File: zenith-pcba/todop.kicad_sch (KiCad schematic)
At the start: 1 part, among them U1 XC7A50T-CSG325

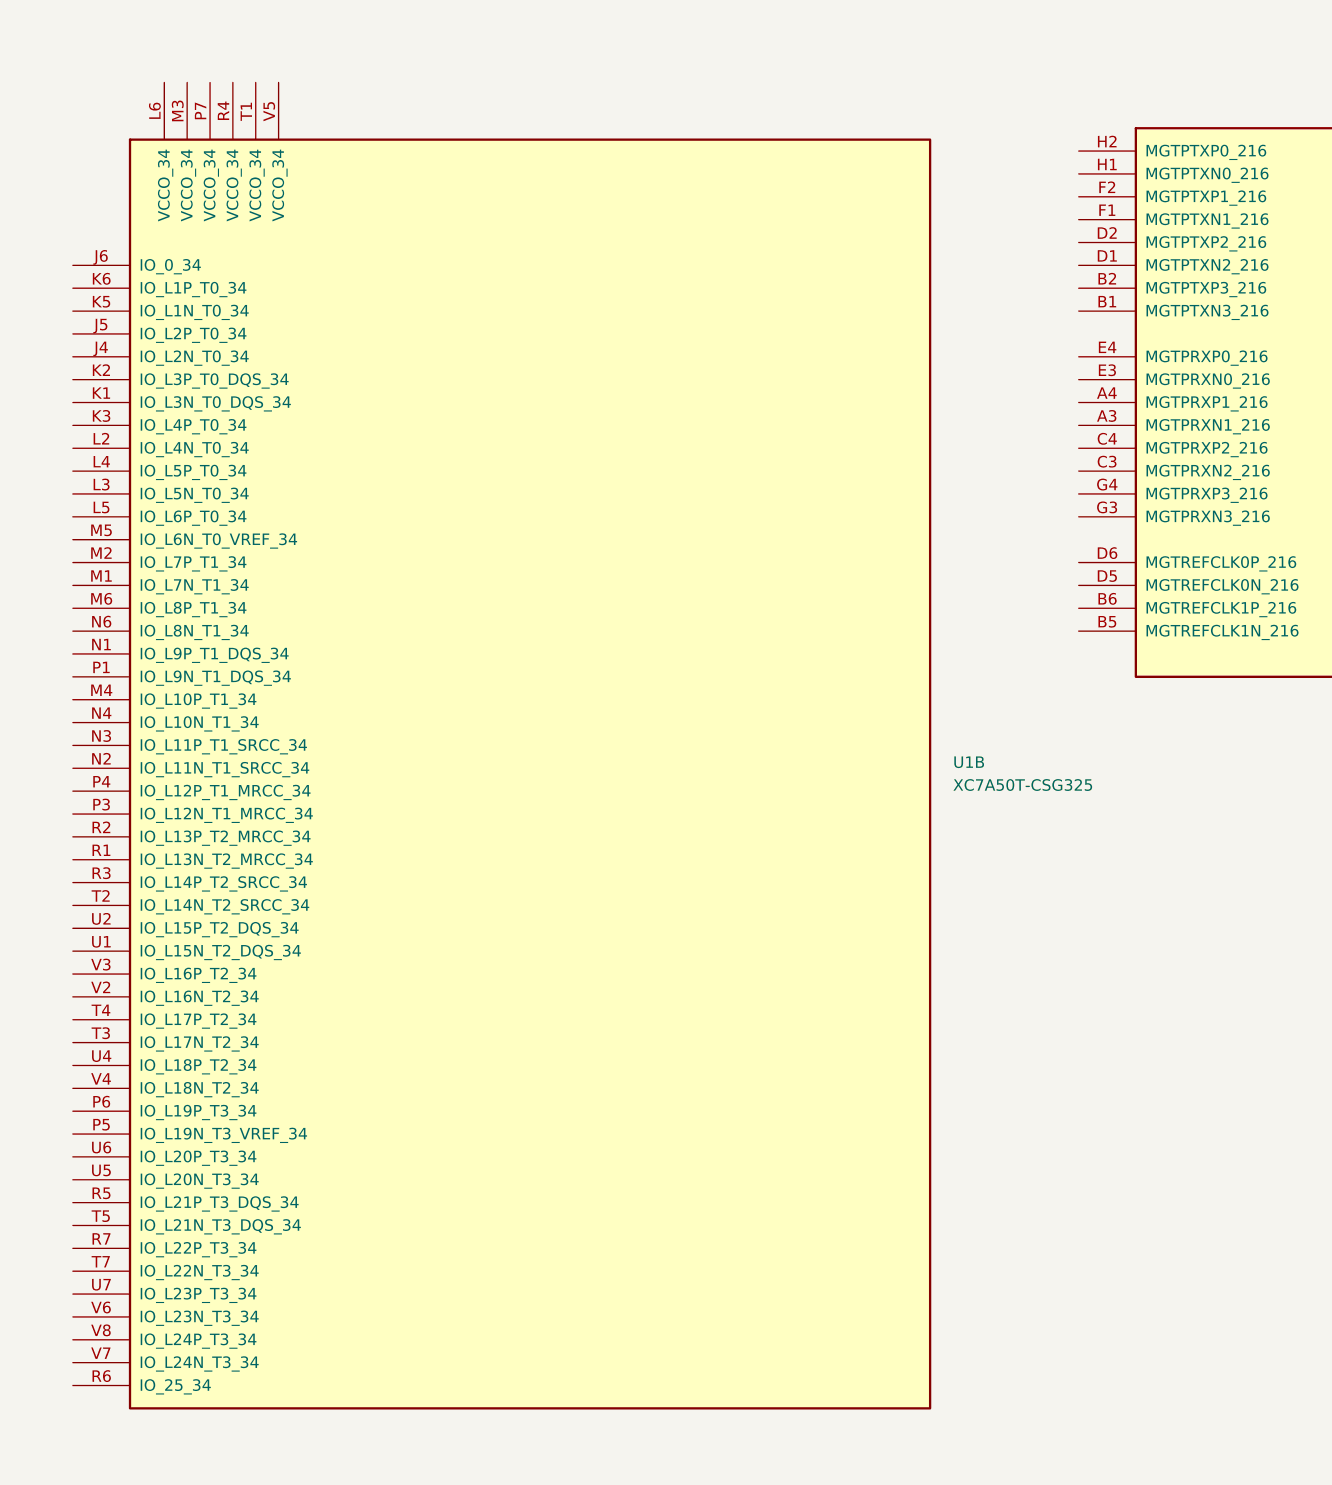
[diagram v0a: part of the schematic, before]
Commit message: feat(pcba): programmer connections and uart
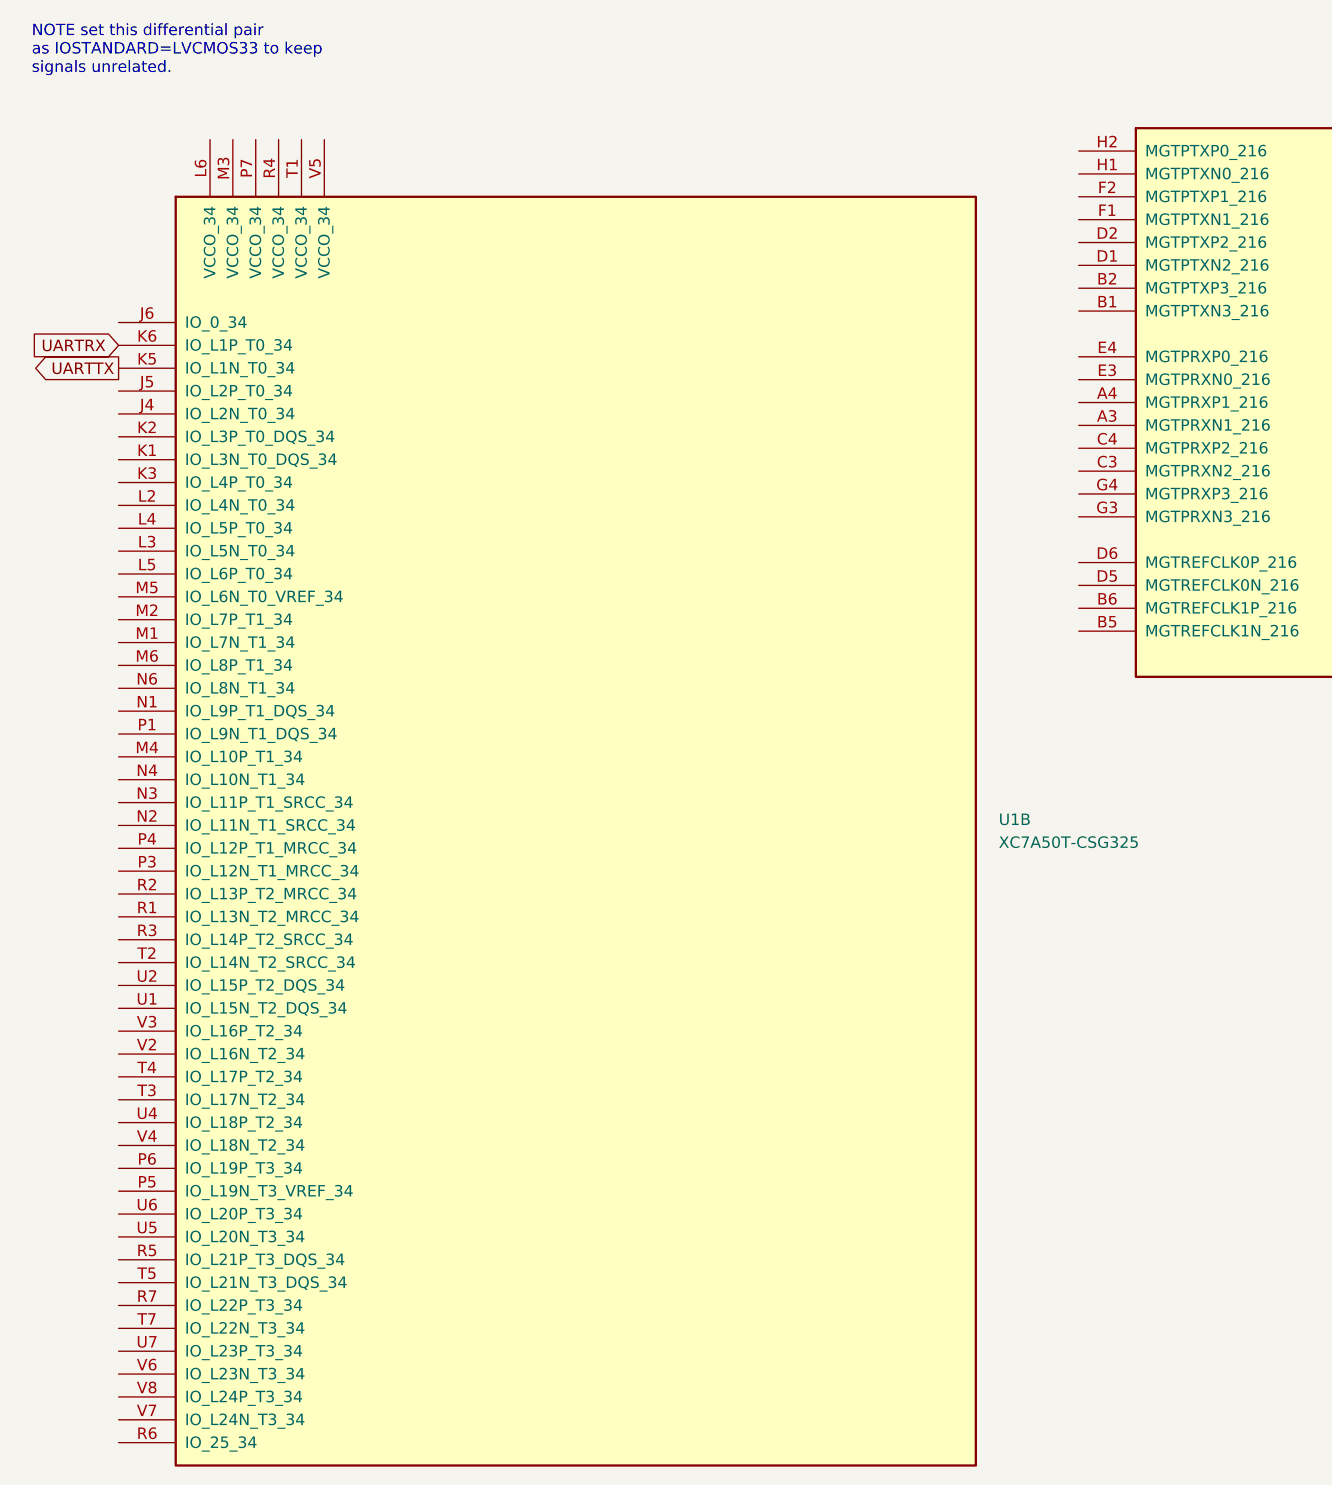
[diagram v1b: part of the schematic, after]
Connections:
- net UARTTX: now reaches U1.K5 (IO_L1N_T0_34)
- net UARTRX: now reaches U1.K6 (IO_L1P_T0_34)
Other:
- note added: "NOTE set this differential pair as IOSTANDARD=LVCMOS33 to keep signals unrelated."
- moved on the sheet: U1B
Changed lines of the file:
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@@
 	(generator_version "10.0")
 	(paper "A4")
+	(text "NOTE set this differential pair\nas IOSTANDARD=LVCMOS33 to keep\nsignals unrelated."
+		(exclude_from_sim yes)
+		(at 13.208 16.764 0)
+		(effects
+			(font
+				(size 1.27 1.27)
+			)
+			(justify left)
+		)
+	)
+	(global_label "UARTTX"
+		(shape output)
+		(at 22.86 52.07 180)
+		(fields_autoplaced yes)
+		(effects
+			(font
+				(size 1.27 1.27)
+			)
+			(justify right)
+		)
+		(property "Intersheetrefs" "${INTERSHEET_REFS}"
+			(at 13.041 52.07 0)
+			(hide yes)
+			(show_name no)
+			(do_not_autoplace no)
+			(effects
+				(font
+					(size 1.27 1.27)
+				)
+				(justify right)
+			)
+		)
+	)
+	(global_label "UARTRX"
+		(shape input)
+		(at 22.86 49.53 180)
+		(fields_autoplaced yes)
+		(effects
+			(font
+				(size 1.27 1.27)
+			)
+			(justify right)
+		)
+		(property "Intersheetrefs" "${INTERSHEET_REFS}"
+			(at 12.7386 49.53 0)
+			(hide yes)
+			(show_name no)
+			(do_not_autoplace no)
+			(effects
+				(font
+					(size 1.27 1.27)
+				)
+				(justify right)
+			)
+		)
+	)
 	(symbol
 		(lib_id "FPGA_Xilinx_Artix7:XC7A50T-CSG325")
@@
 	(symbol
 		(lib_id "FPGA_Xilinx_Artix7:XC7A50T-CSG325")
-		(at 68.58 93.98 0)
+		(at 73.66 100.33 0)
 		(unit 2)
 		(body_style 1)
@@
 		(fields_autoplaced yes)
 		(property "Reference" "U1"
-			(at 115.57 95.8849 0)
+			(at 120.65 102.2349 0)
 			(show_name no)
 			(do_not_autoplace no)
@@
 		)
 		(property "Value" "XC7A50T-CSG325"
-			(at 115.57 98.4249 0)
+			(at 120.65 104.7749 0)
 			(show_name no)
 			(do_not_autoplace no)
@@
 		)
 		(property "Footprint" "Package_BGA:Xilinx_CSG325"
-			(at 68.58 93.98 0)
+			(at 73.66 100.33 0)
 			(hide yes)
 			(show_name no)
@@
 		)
 		(property "Datasheet" ""
-			(at 68.58 93.98 0)
+			(at 73.66 100.33 0)
 			(show_name no)
 			(do_not_autoplace no)
@@
 		)
 		(property "Description" "Artix 7 T 50 XC7A50T-CSG325"
-			(at 68.58 93.98 0)
+			(at 73.66 100.33 0)
 			(hide yes)
 			(show_name no)

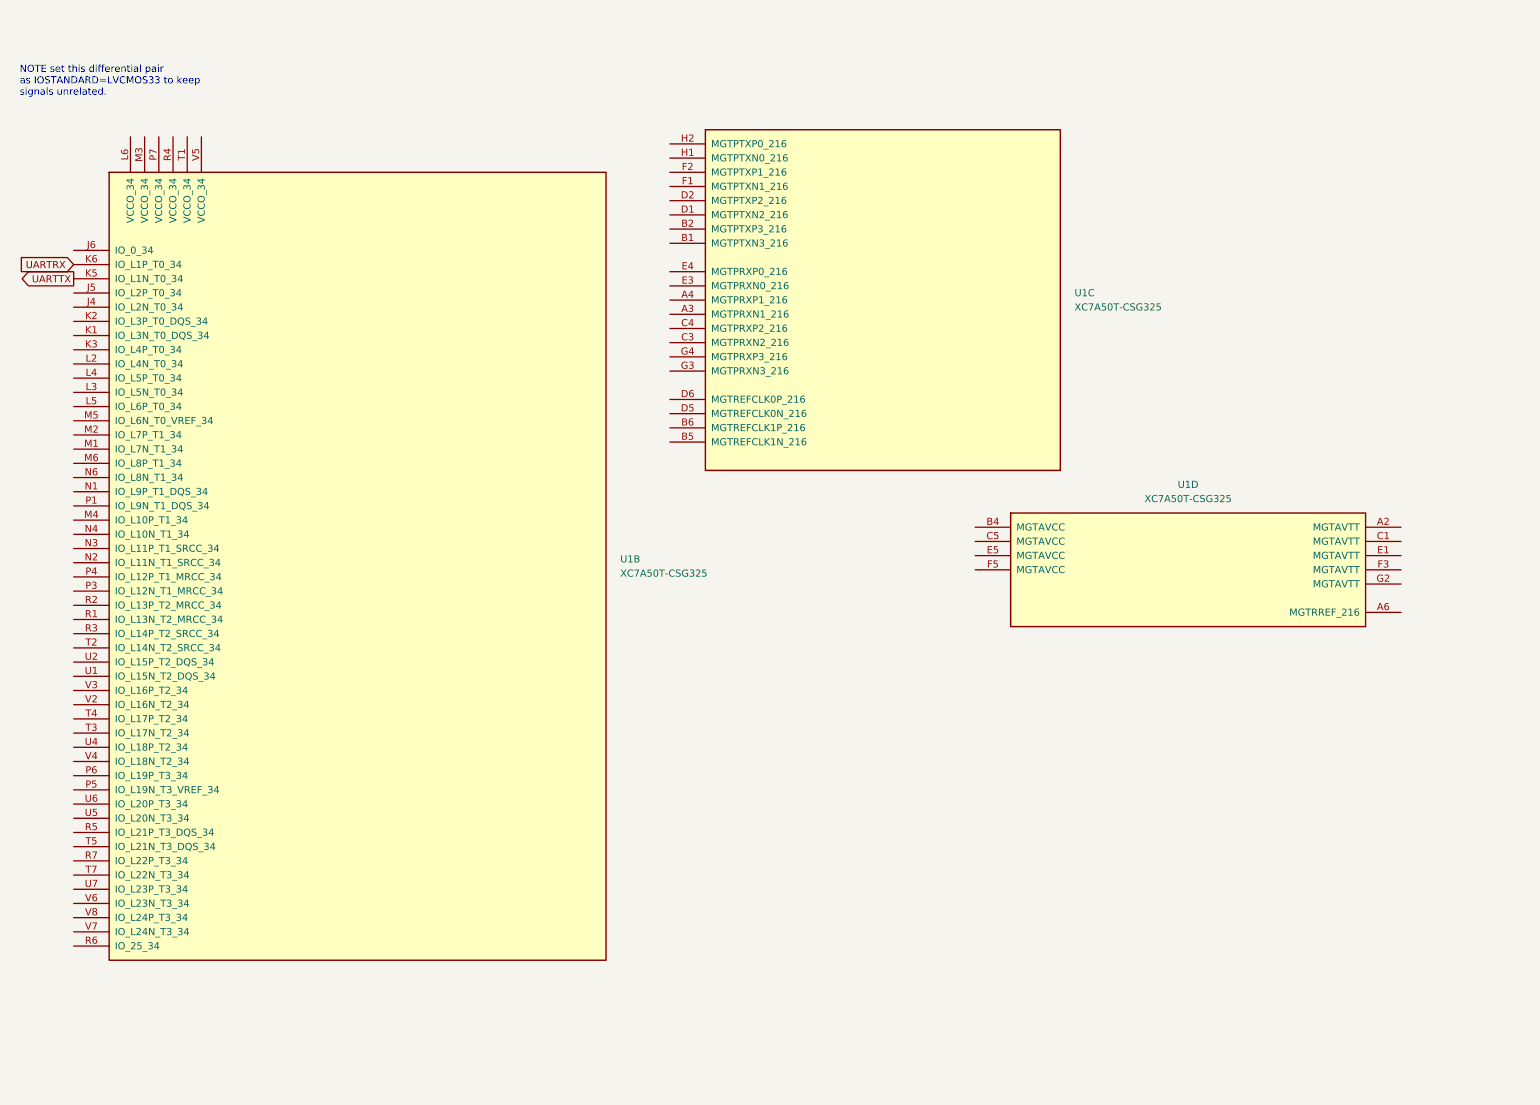
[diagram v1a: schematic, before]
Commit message: chore(pcba): import din connectors
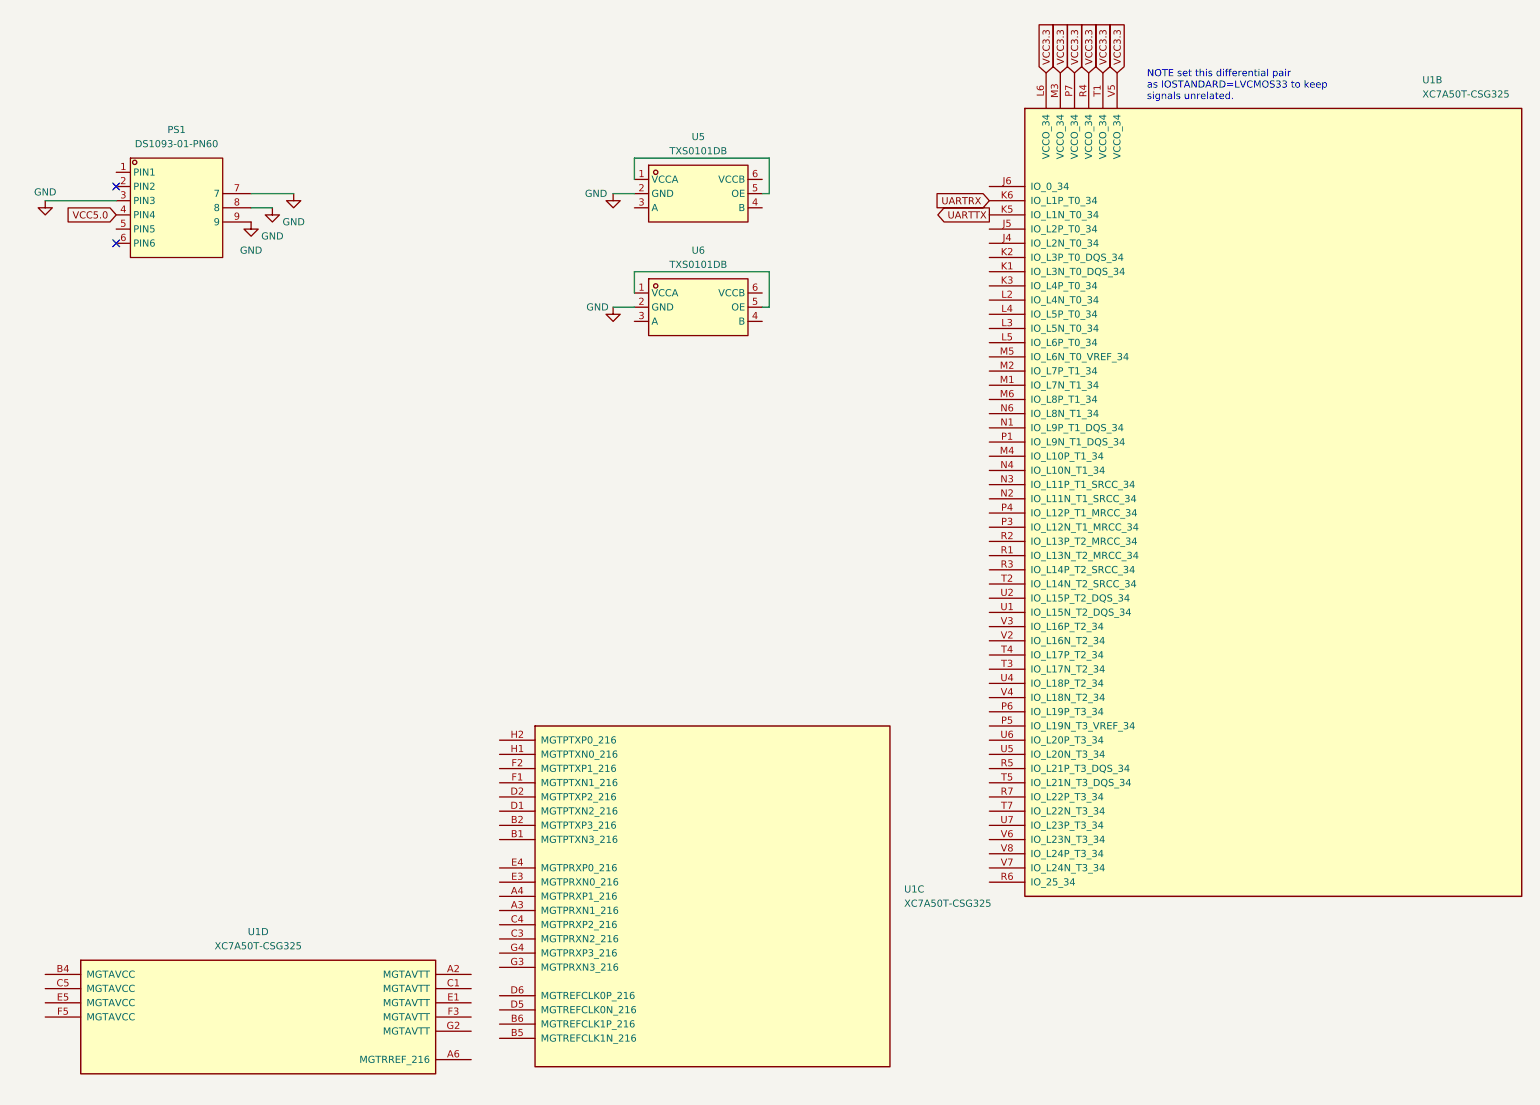
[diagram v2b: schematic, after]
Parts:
- added PS1: DS1093-01-PN60, easyeda2kicad:CONN-TH_DS1093-01-PN60, symbol easyeda2kicad:DS1093-01-PN60
- added U5, U6: TXS0101DB, easyeda2kicad:SOT-23-6_L2.9-W1.6-P0.95-LS2.9-BL, symbol easyeda2kicad:TXS0101DB
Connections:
- net VCC3.3: now reaches U1.L6 (VCCO_34)
- net VCC3.3: now also U1.M3 (VCCO_34), U1.P7 (VCCO_34), U1.R4 (VCCO_34), U1.T1 (VCCO_34), U1.V5 (VCCO_34)
- new net: U6.1 (VCCA), U6.5 (OE)
- new net: U5.1 (VCCA), U5.5 (OE)
- new net GND: PS1.3 (PIN3), PS1.7, PS1.8, PS1.9, U5.2 (GND), U6.2 (GND)
- new net VCC5.0: PS1.4 (PIN4)
- no-connect marks 0 -> 2
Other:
- moved on the sheet: U1B, U1C, U1D
